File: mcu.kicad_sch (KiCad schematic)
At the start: 3 parts, among them U1 ESP32-S3-WROOM-1

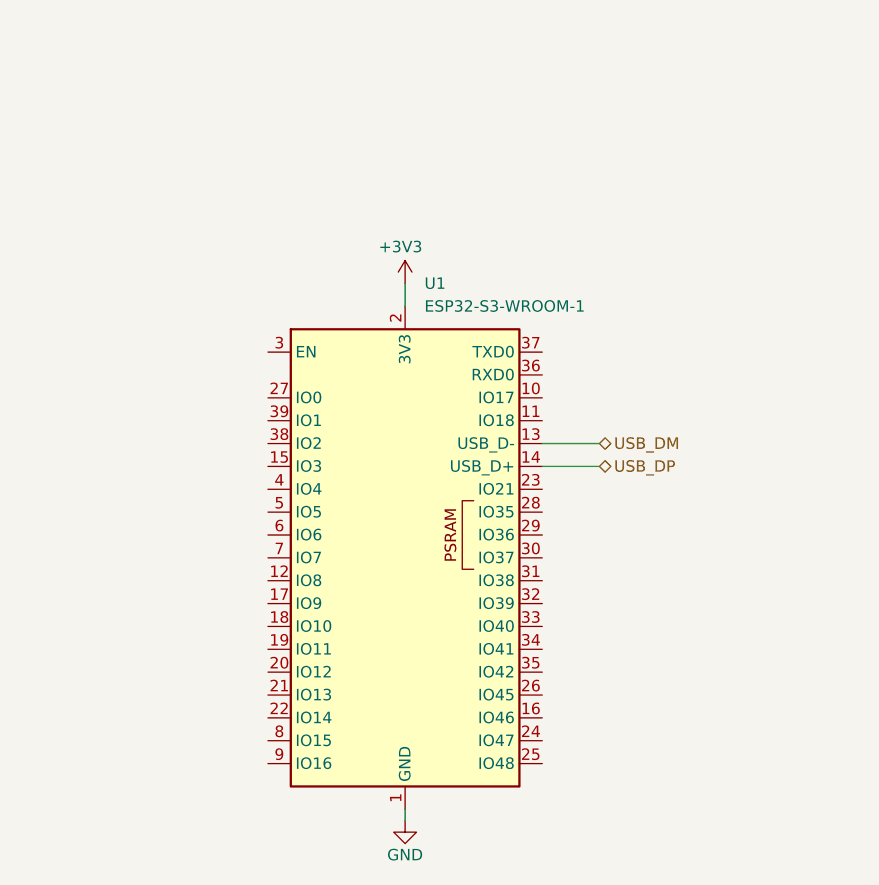
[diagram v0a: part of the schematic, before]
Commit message: component placement inside schematic
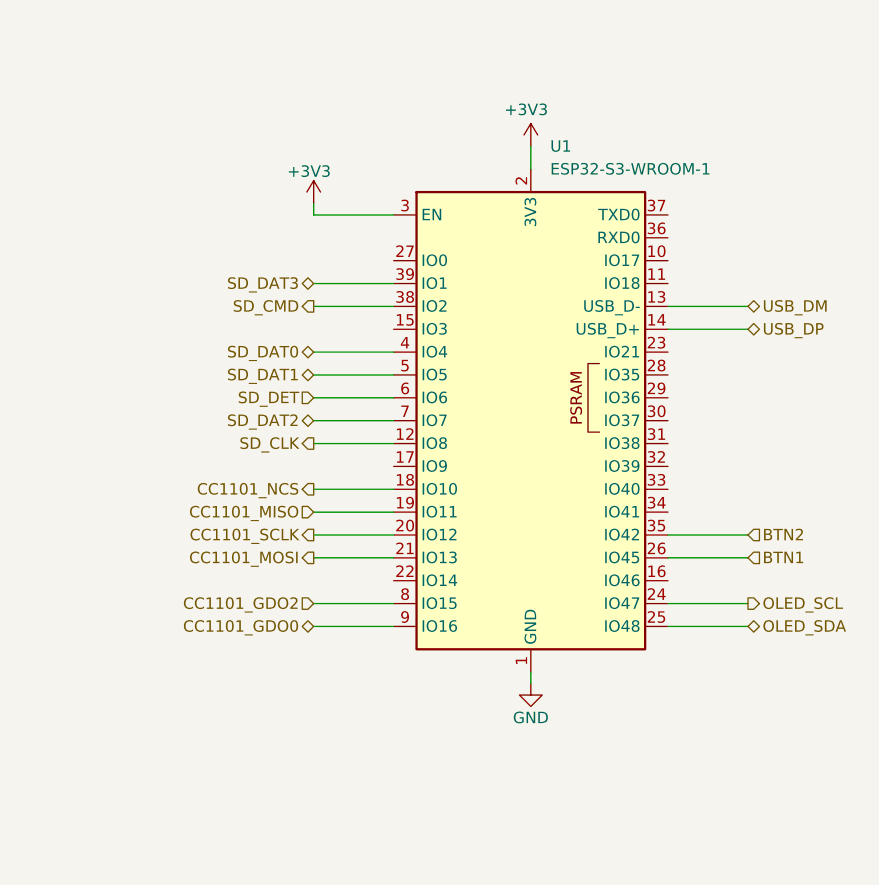
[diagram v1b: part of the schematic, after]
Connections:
- net +3V3: now also U1.3 (EN)
- net SD_CLK: now reaches U1.12 (IO8)
- net CC1101_NCS: now reaches U1.18 (IO10)
- net CC1101_MISO: now reaches U1.19 (IO11)
- net CC1101_SCLK: now reaches U1.20 (IO12)
- net CC1101_MOSI: now reaches U1.21 (IO13)
- net OLED_SCL: now reaches U1.24 (IO47)
- net OLED_SDA: now reaches U1.25 (IO48)
- net BTN1: now reaches U1.26 (IO45)
- net BTN2: now reaches U1.35 (IO42)
- net SD_CMD: now reaches U1.38 (IO2)
- net SD_DAT3: now reaches U1.39 (IO1)
- net SD_DAT0: now reaches U1.4 (IO4)
- net SD_DAT1: now reaches U1.5 (IO5)
- net SD_DET: now reaches U1.6 (IO6)
- net SD_DAT2: now reaches U1.7 (IO7)
- net CC1101_GDO2: now reaches U1.8 (IO15)
- net CC1101_GDO0: now reaches U1.9 (IO16)
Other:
- moved on the sheet: U1

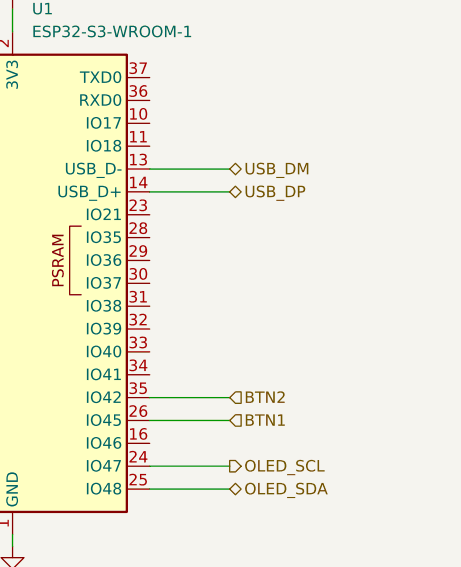
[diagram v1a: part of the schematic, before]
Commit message: add esd usb protections
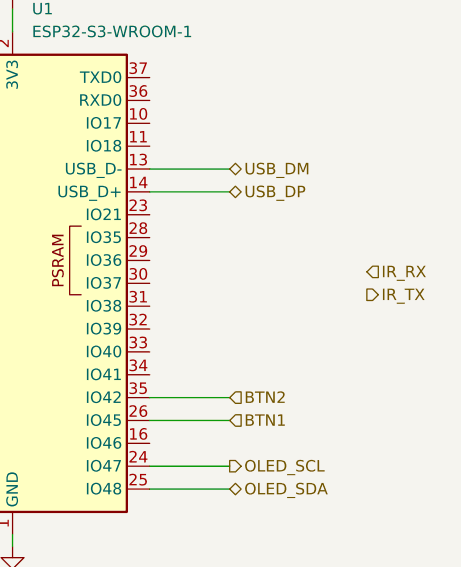
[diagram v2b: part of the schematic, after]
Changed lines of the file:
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@@
+		)
+	)
+	(hierarchical_label "IR_RX"
+		(shape input)
+		(at 180.34 91.44 0)
+		(effects
+			(font
+				(size 1.27 1.27)
+			)
+			(justify left)
 		)
 	)
@@
 		(effects
 			(font
+				(size 1.27 1.27)
+			)
+			(justify left)
+		)
+	)
+	(hierarchical_label "IR_TX"
+		(shape output)
+		(at 180.34 93.98 0)
+		(effects
+			(font

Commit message: fix rgb led labels
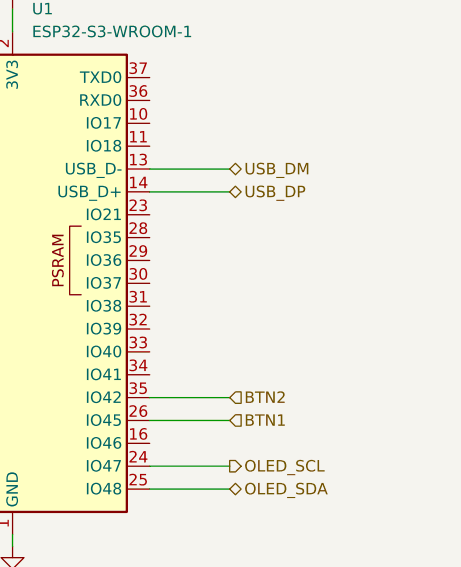
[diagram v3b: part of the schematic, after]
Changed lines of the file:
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@@
-		)
-	)
-	(hierarchical_label "IR_RX"
-		(shape input)
-		(at 180.34 91.44 0)
-		(effects
-			(font
-				(size 1.27 1.27)
-			)
-			(justify left)
 		)
 	)
@@
 		(effects
 			(font
-				(size 1.27 1.27)
-			)
-			(justify left)
-		)
-	)
-	(hierarchical_label "IR_TX"
-		(shape output)
-		(at 180.34 93.98 0)
-		(effects
-			(font

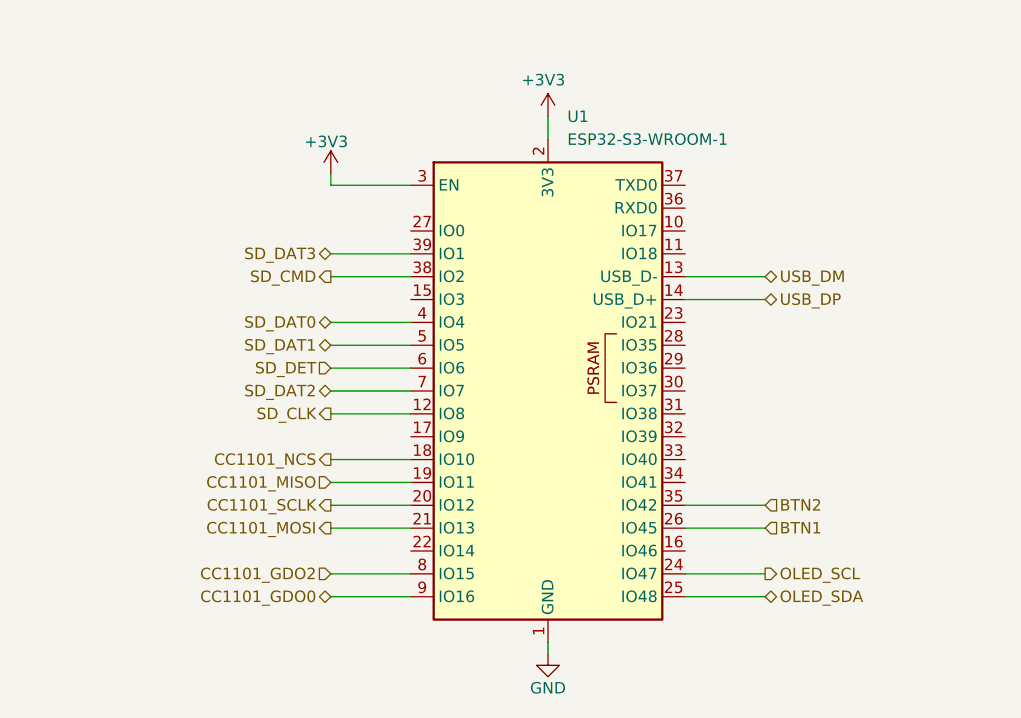
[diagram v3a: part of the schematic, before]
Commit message: add external gpio connector
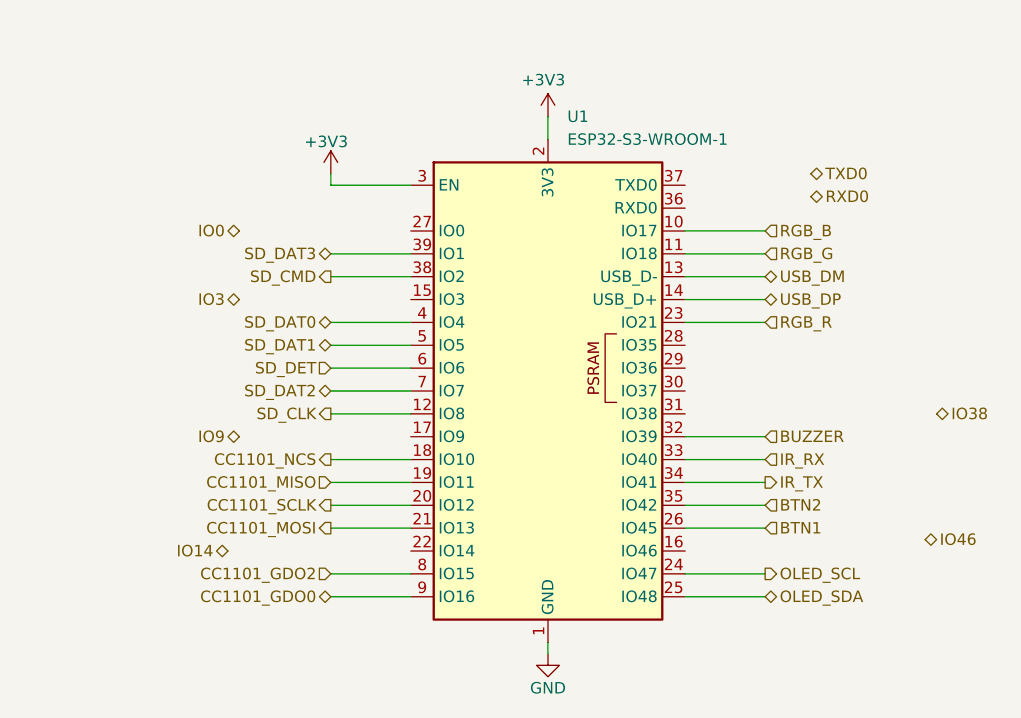
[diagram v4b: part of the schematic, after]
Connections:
- net RGB_B: now reaches U1.10 (IO17)
- net RGB_G: now reaches U1.11 (IO18)
- net RGB_R: now reaches U1.23 (IO21)
- net BUZZER: now reaches U1.32 (IO39)
- net IR_RX: now reaches U1.33 (IO40)
- net IR_TX: now reaches U1.34 (IO41)
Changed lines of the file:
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@@
+	(wire
+		(pts
+			(xy 165.1 97.79) (xy 156.21 97.79)
+		)
+		(stroke
+			(width 0)
+			(type default)
+		)
+	)
 	(wire
 		(pts
@@
 	(wire
 		(pts
+			(xy 165.1 77.47) (xy 156.21 77.47)
+		)
+		(stroke
+			(width 0)
+			(type default)
+		)
+	)
+	(wire
+		(pts
 			(xy 116.84 107.95) (xy 125.73 107.95)
 		)
@@
 	(wire
 		(pts
+			(xy 165.1 102.87) (xy 156.21 102.87)
+		)
+		(stroke
+			(width 0)
+			(type default)
+		)
+	)
+	(wire
+		(pts
 			(xy 46.99 59.69) (xy 46.99 60.96)
 		)
@@
 	(wire
 		(pts
+			(xy 165.1 85.09) (xy 156.21 85.09)
+		)
+		(stroke
+			(width 0)
+			(type default)
+		)
+	)
+	(wire
+		(pts
 			(xy 116.84 77.47) (xy 125.73 77.47)
 		)
@@
 	(wire
 		(pts
+			(xy 165.1 74.93) (xy 156.21 74.93)
+		)
+		(stroke
+			(width 0)
+			(type default)
+		)
+	)
+	(wire
+		(pts
 			(xy 116.84 113.03) (xy 125.73 113.03)
 		)
@@
 	(wire
 		(pts
+			(xy 165.1 100.33) (xy 156.21 100.33)
+		)
+		(stroke
+			(width 0)
+			(type default)
+		)
+	)
+	(wire
+		(pts
 			(xy 116.84 105.41) (xy 125.73 105.41)
 		)
@@
 		)
 	)
+	(hierarchical_label "RGB_B"
+		(shape input)
+		(at 165.1 74.93 0)
+		(effects
+			(font
+				(size 1.27 1.27)
+			)
+			(justify left)
+		)
+	)
+	(hierarchical_label "RGB_R"
+		(shape input)
+		(at 165.1 85.09 0)
+		(effects
+			(font
+				(size 1.27 1.27)
+			)
+			(justify left)
+		)
+	)
+	(hierarchical_label "BUZZER"
+		(shape input)
+		(at 165.1 97.79 0)
+		(effects
+			(font
+				(size 1.27 1.27)
+			)
+			(justify left)
+		)
+	)
+	(hierarchical_label "IO3"
+		(shape bidirectional)
+		(at 106.68 82.55 180)
+		(effects
+			(font
+				(size 1.27 1.27)
+			)
+			(justify right)
+		)
+	)
+	(hierarchical_label "IO9"
+		(shape bidirectional)
+		(at 106.68 97.79 180)
+		(effects
+			(font
+				(size 1.27 1.27)
+			)
+			(justify right)
+		)
+	)
+	(hierarchical_label "TXD0"
+		(shape bidirectional)
+		(at 170.18 68.58 0)
+		(effects
+			(font
+				(size 1.27 1.27)
+			)
+			(justify left)
+		)
+	)
 	(hierarchical_label "USB_DP"
 		(shape bidirectional)
@@
 		)
 	)
+	(hierarchical_label "RXD0"
+		(shape bidirectional)
+		(at 170.18 71.12 0)
+		(effects
+			(font
+				(size 1.27 1.27)
+			)
+			(justify left)
+		)
+	)
 	(hierarchical_label "USB_DM"
 		(shape bidirectional)
 		(at 165.1 80.01 0)
+		(effects
+			(font
+				(size 1.27 1.27)
+			)
+			(justify left)
+		)
+	)
+	(hierarchical_label "IO38"
+		(shape bidirectional)
+		(at 184.15 95.25 0)
 		(effects
 			(font
@@
 		)
 	)
+	(hierarchical_label "IO46"
+		(shape bidirectional)
+		(at 182.88 109.22 0)
+		(effects
+			(font
+				(size 1.27 1.27)
+			)
+			(justify left)
+		)
+	)
+	(hierarchical_label "IR_TX"
+		(shape output)
+		(at 165.1 102.87 0)
+		(effects
+			(font
+				(size 1.27 1.27)
+			)
+			(justify left)
+		)
+	)
 	(hierarchical_label "CC1101_MOSI"
 		(shape output)
@@
 		)
 	)
+	(hierarchical_label "IR_RX"
+		(shape input)
+		(at 165.1 100.33 0)
+		(effects
+			(font
+				(size 1.27 1.27)
+			)
+			(justify left)
+		)
+	)
 	(hierarchical_label "CC1101_MISO"
 		(shape input)
@@
 			)
 			(justify right)
+		)
+	)
+	(hierarchical_label "RGB_G"
+		(shape input)
+		(at 165.1 77.47 0)
+		(effects
+			(font
+				(size 1.27 1.27)
+			)
+			(justify left)
 		)
 	)
@@
 		)
 	)
+	(hierarchical_label "IO0"
+		(shape bidirectional)
+		(at 106.68 74.93 180)
+		(effects
+			(font
+				(size 1.27 1.27)
+			)
+			(justify right)
+		)
+	)
 	(hierarchical_label "CC1101_SCLK"
 		(shape output)
@@
 		)
 	)
+	(hierarchical_label "IO14"
+		(shape bidirectional)
+		(at 105.41 110.49 180)
+		(effects
+			(font
+				(size 1.27 1.27)
+			)
+			(justify right)
+		)
+	)

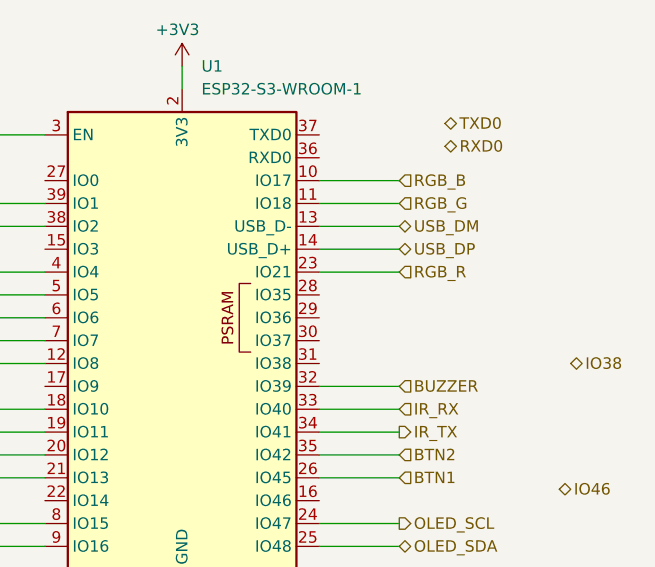
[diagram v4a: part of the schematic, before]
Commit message: add usbc esd protections
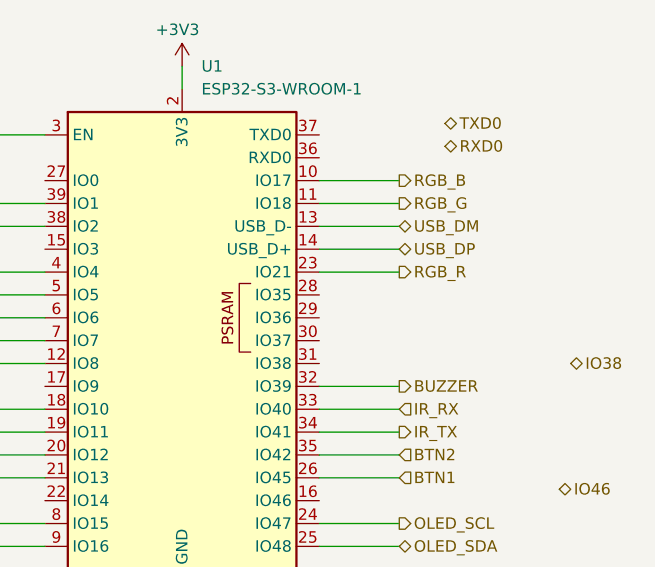
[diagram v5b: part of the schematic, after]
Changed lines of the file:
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@@
 	)
 	(hierarchical_label "RGB_B"
-		(shape input)
+		(shape output)
 		(at 165.1 74.93 0)
 		(effects
@@
 	)
 	(hierarchical_label "RGB_R"
-		(shape input)
+		(shape output)
 		(at 165.1 85.09 0)
 		(effects
@@
 	)
 	(hierarchical_label "BUZZER"
-		(shape input)
+		(shape output)
 		(at 165.1 97.79 0)
 		(effects
@@
 	)
 	(hierarchical_label "RGB_G"
-		(shape input)
+		(shape output)
 		(at 165.1 77.47 0)
 		(effects

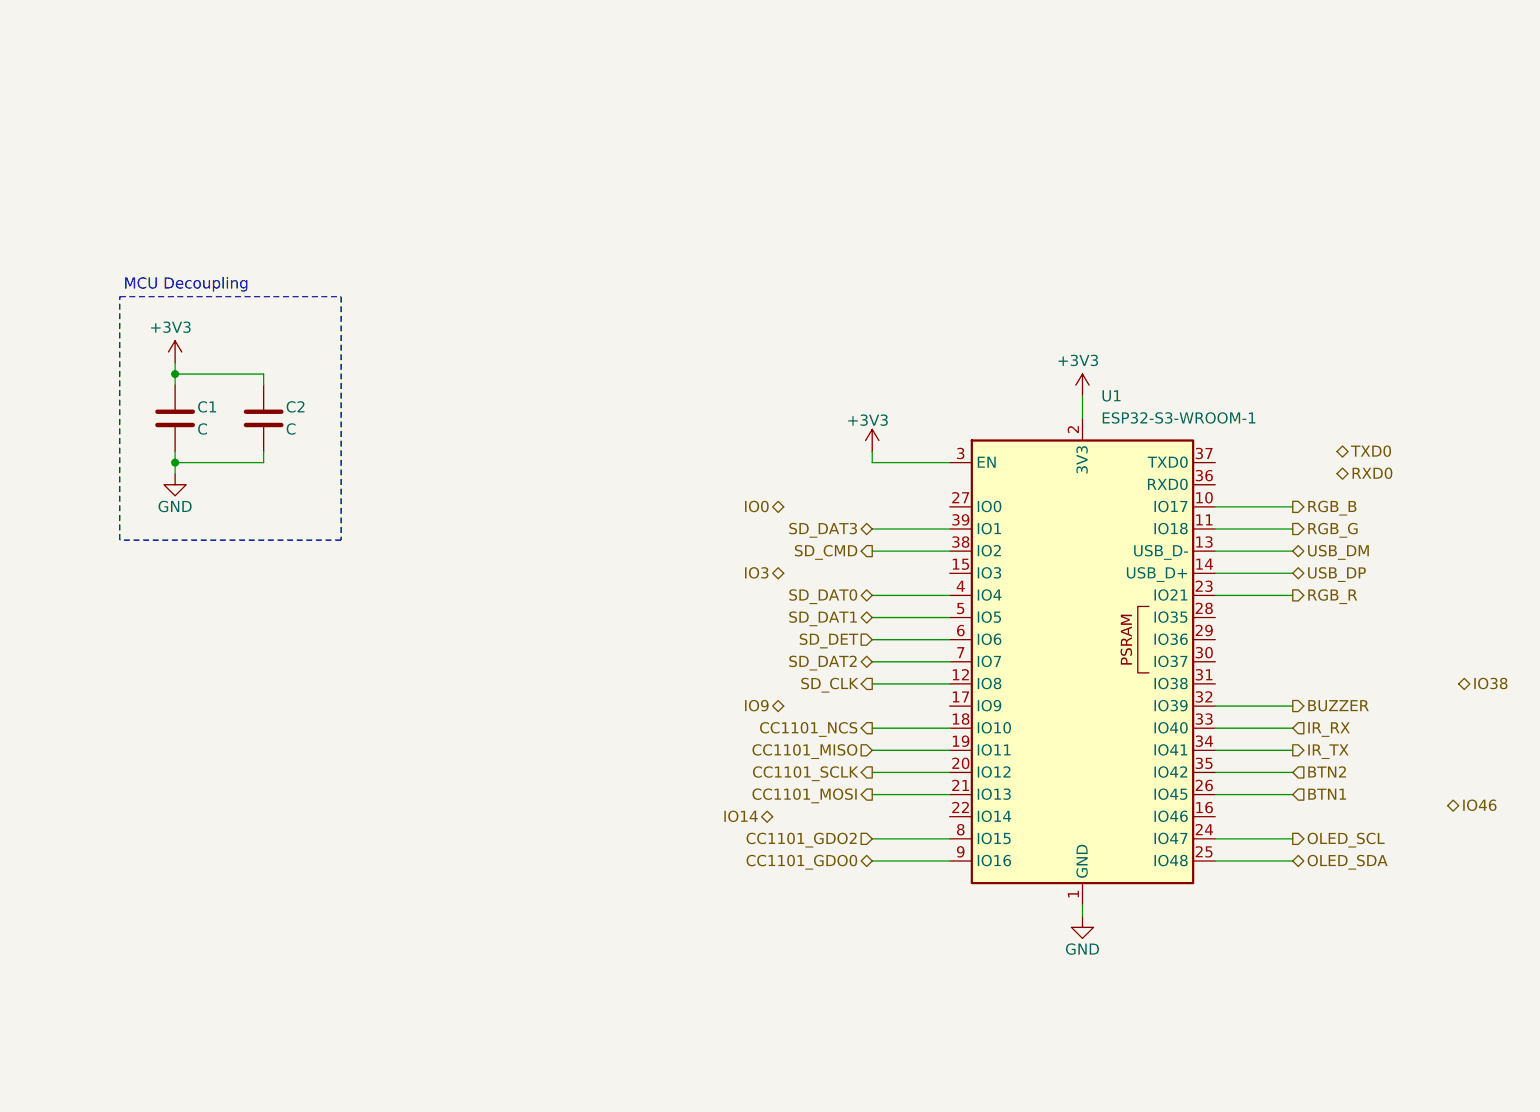
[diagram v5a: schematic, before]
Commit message: add missing connections inside MCU
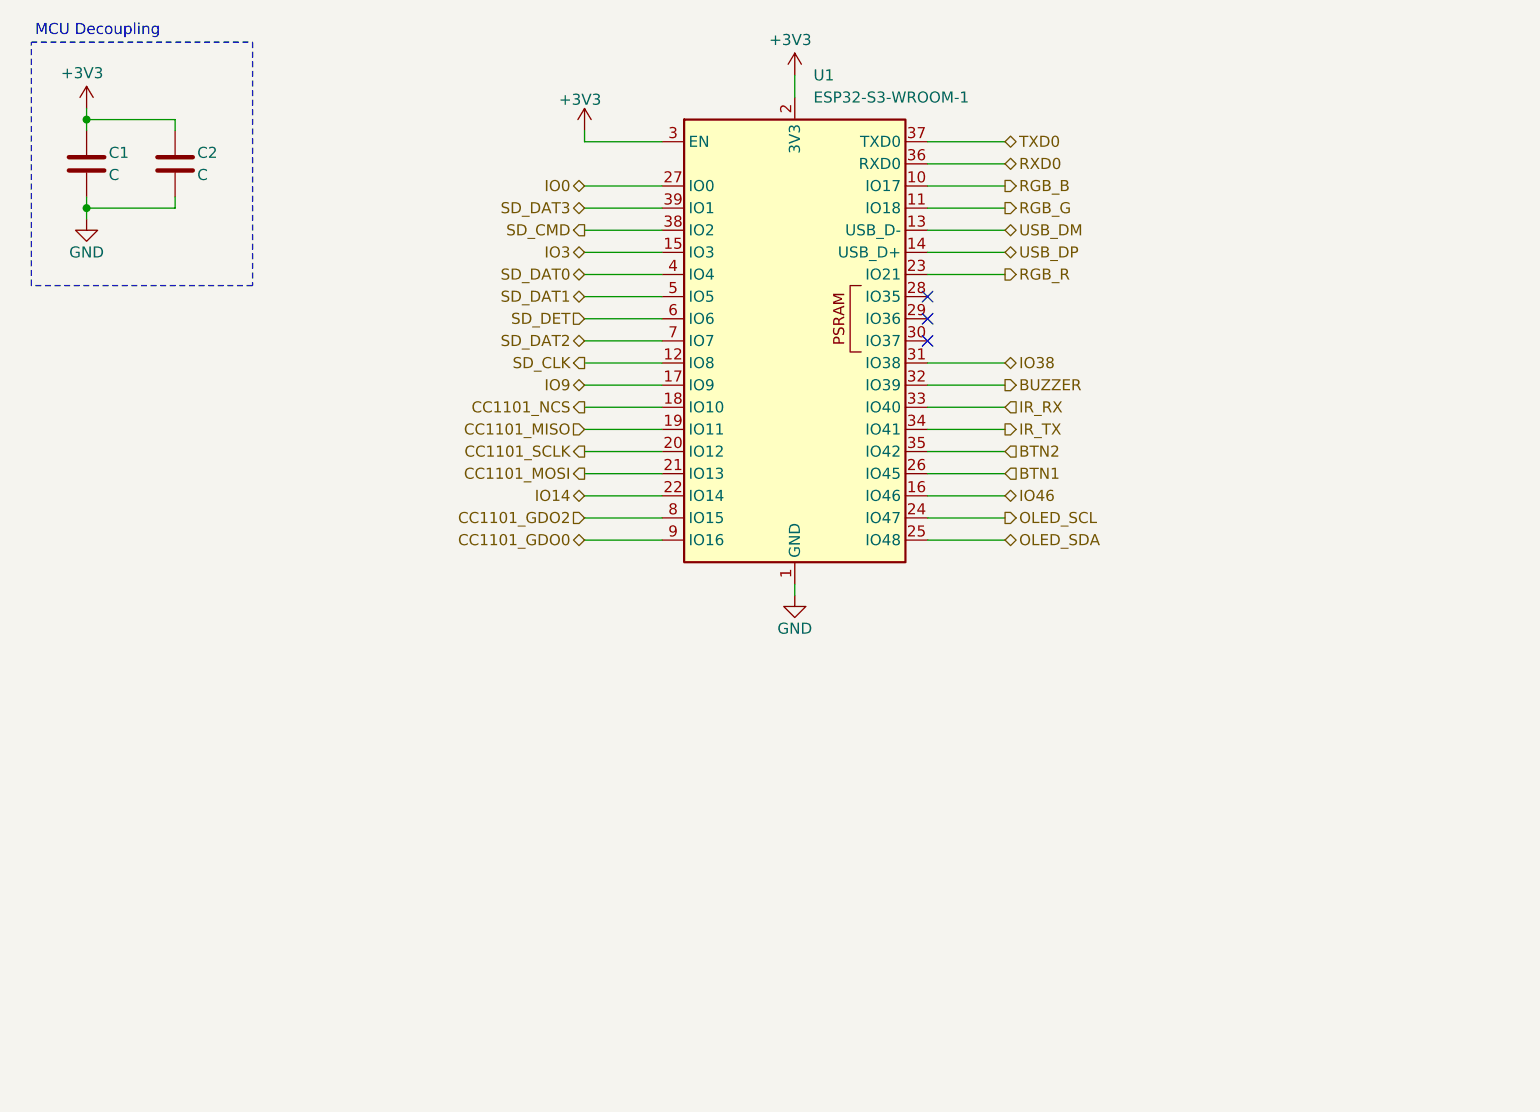
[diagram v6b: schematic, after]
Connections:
- net IO0: now also U1.27 (IO0)
- net IO14: now also U1.22 (IO14)
- net IO3: now also U1.15 (IO3)
- net IO38: now also U1.31 (IO38)
- net IO46: now also U1.16 (IO46)
- net IO9: now also U1.17 (IO9)
- net RXD0: now also U1.36 (RXD0)
- net TXD0: now also U1.37 (TXD0)
- no-connect marks 0 -> 3
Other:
- moved on the sheet: C1, C2, U1
